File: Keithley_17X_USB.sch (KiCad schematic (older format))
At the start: 37 parts, among them J1 USB_B, J2 SIGNAL INPUT, J3 PROG, U1 TLP281-4, U2 TLP281-4, U3 MIC5504-3.3YM5, U4 MSP430FR2110, U5 FT230XS

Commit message: add more footprints and 3d models
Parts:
- D1: footprint (none) -> TI_TVSDiode:TI_PX1SON_DPY
- D3: value D_Schottky -> DSS16UTR; footprint (none) -> SMC_Diodes:D_SOD-123FL
- H1, H2, H3, H4: value CaseMnt -> M3
- J2: footprint (none) -> Connector_PinHeader_2.54mm:PinHeader_2x07_P2.54mm_Horizontal
- J3: footprint (none) -> Connector_PinHeader_2.54mm:PinHeader_1x04_P2.54mm_Vertical
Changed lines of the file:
@@
 P 2350 1000
 F 0 "D3" H 2350 1100 50  0000 C CNN
-F 1 "D_Schottky" H 2350 900 50  0000 C CNN
-F 2 "" H 2350 1000 50  0001 C CNN
+F 1 "DSS16UTR" H 2350 900 50  0000 C CNN
+F 2 "SMC_Diodes:D_SOD-123FL" H 2350 1000 50  0001 C CNN
 F 3 "http://www.smc-diodes.com/propdf/DSS12U%20THRU%20DSS125U%20N1873%20REV.A.pdf" H 2350 1000 50  0001 C CNN
 F 4 "SCHOTTKY 60V SOD-123FL" H 2350 1000 50  0001 C CNN "Description"
@@
 F 0 "D1" V 1250 1950 50  0000 C CNN
 F 1 "TPD1E10B06" H 1250 1750 50  0000 C CNN
-F 2 "" H 1250 1850 50  0001 C CNN
+F 2 "TI_TVSDiode:TI_PX1SON_DPY" H 1250 1850 50  0001 C CNN
 F 3 "http://www.ti.com/lit/ds/symlink/tpd1e10b06-q1.pdf" H 1250 1850 50  0001 C CNN
 F 4 "TVS DIODE 5.5V 14V 2X1SON" H 1250 1850 50  0001 C CNN "Description"
@@
 F 0 "J2" H 1600 5500 50  0000 C CNN
 F 1 "SIGNAL INPUT" H 1600 4700 50  0000 C CNN
-F 2 "" H 1550 5100 50  0001 C CNN
+F 2 "Connector_PinHeader_2.54mm:PinHeader_2x07_P2.54mm_Horizontal" H 1550 5100 50  0001 C CNN
 F 3 "http://www.on-shore.com/wp-content/uploads/2015/09/302-rxxx.pdf" H 1550 5100 50  0001 C CNN
 F 4 "CONN HEADER R/A 14POS 2.54MM" H 1550 5100 50  0001 C CNN "Description"
@@
 F 0 "J3" H 4950 3850 50  0000 C CNN
 F 1 "PROG" H 4950 3350 50  0000 C CNN
-F 2 "" H 4950 3650 50  0001 C CNN
+F 2 "Connector_PinHeader_2.54mm:PinHeader_1x04_P2.54mm_Vertical" H 4950 3650 50  0001 C CNN
 F 3 "~" H 4950 3650 50  0001 C CNN
 	1    4950 3650
@@
 P 5300 5950
 F 0 "H1" H 5300 6200 50  0000 C CNN
-F 1 "CaseMnt" H 5300 6125 50  0000 C CNN
+F 1 "M3" H 5300 6125 50  0000 C CNN
 F 2 "" H 5300 5950 50  0001 C CNN
 F 3 "~" H 5300 5950 50  0001 C CNN
@@
 P 5700 5950
 F 0 "H2" H 5700 6200 50  0000 C CNN
-F 1 "CaseMnt" H 5700 6125 50  0000 C CNN
+F 1 "M3" H 5700 6125 50  0000 C CNN
 F 2 "" H 5700 5950 50  0001 C CNN
 F 3 "~" H 5700 5950 50  0001 C CNN
@@
 P 6100 5950
 F 0 "H3" H 6100 6200 50  0000 C CNN
-F 1 "CaseMnt" H 6100 6125 50  0000 C CNN
+F 1 "M3" H 6100 6125 50  0000 C CNN
 F 2 "" H 6100 5950 50  0001 C CNN
 F 3 "~" H 6100 5950 50  0001 C CNN
@@
 P 6500 5950
 F 0 "H4" H 6500 6200 50  0000 C CNN
-F 1 "CaseMnt" H 6500 6125 50  0000 C CNN
+F 1 "M3" H 6500 6125 50  0000 C CNN
 F 2 "" H 6500 5950 50  0001 C CNN
 F 3 "~" H 6500 5950 50  0001 C CNN

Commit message: add r_array footprint and 3d model
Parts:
- H1, H2, H3, H4: footprint (none) -> MountingHole:MountingHole_3.2mm_M3_DIN965_Pad
- RN1, RN2: footprint (none) -> R_Array_Convex:YC324-JK-0710KL
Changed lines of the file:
@@
 F 0 "RN1" V 2250 4650 50  0000 C CNN
 F 1 "10k" V 2750 4650 50  0000 C CNN
-F 2 "" V 2825 4650 50  0001 C CNN
+F 2 "R_Array_Convex:YC324-JK-0710KL" V 2825 4650 50  0001 C CNN
 F 3 "https://media.digikey.com/pdf/Data%20Sheets/Yageo%20PDFs/YC102-358,TC122-164_Series_DS.pdf" H 2550 4650 50  0001 C CNN
 F 4 "RES ARRAY 4 RES 10K OHM 2012" H 2550 4650 50  0001 C CNN "Description"
@@
 F 0 "RN2" V 2250 7450 50  0000 C CNN
 F 1 "10k" V 2750 7450 50  0000 C CNN
-F 2 "" V 2825 7450 50  0001 C CNN
+F 2 "R_Array_Convex:YC324-JK-0710KL" V 2825 7450 50  0001 C CNN
 F 3 "https://media.digikey.com/pdf/Data%20Sheets/Yageo%20PDFs/YC102-358,TC122-164_Series_DS.pdf" H 2550 7450 50  0001 C CNN
 F 4 "RES ARRAY 4 RES 10K OHM 2012" H 2550 7450 50  0001 C CNN "Description"
@@
 F 0 "H1" H 5300 6200 50  0000 C CNN
 F 1 "M3" H 5300 6125 50  0000 C CNN
-F 2 "" H 5300 5950 50  0001 C CNN
+F 2 "MountingHole:MountingHole_3.2mm_M3_DIN965_Pad" H 5300 5950 50  0001 C CNN
 F 3 "~" H 5300 5950 50  0001 C CNN
 	1    5300 5950
@@
 F 0 "H2" H 5700 6200 50  0000 C CNN
 F 1 "M3" H 5700 6125 50  0000 C CNN
-F 2 "" H 5700 5950 50  0001 C CNN
+F 2 "MountingHole:MountingHole_3.2mm_M3_DIN965_Pad" H 5700 5950 50  0001 C CNN
 F 3 "~" H 5700 5950 50  0001 C CNN
 	1    5700 5950
@@
 F 0 "H3" H 6100 6200 50  0000 C CNN
 F 1 "M3" H 6100 6125 50  0000 C CNN
-F 2 "" H 6100 5950 50  0001 C CNN
+F 2 "MountingHole:MountingHole_3.2mm_M3_DIN965_Pad" H 6100 5950 50  0001 C CNN
 F 3 "~" H 6100 5950 50  0001 C CNN
 	1    6100 5950
@@
 F 0 "H4" H 6500 6200 50  0000 C CNN
 F 1 "M3" H 6500 6125 50  0000 C CNN
-F 2 "" H 6500 5950 50  0001 C CNN
+F 2 "MountingHole:MountingHole_3.2mm_M3_DIN965_Pad" H 6500 5950 50  0001 C CNN
 F 3 "~" H 6500 5950 50  0001 C CNN
 	1    6500 5950

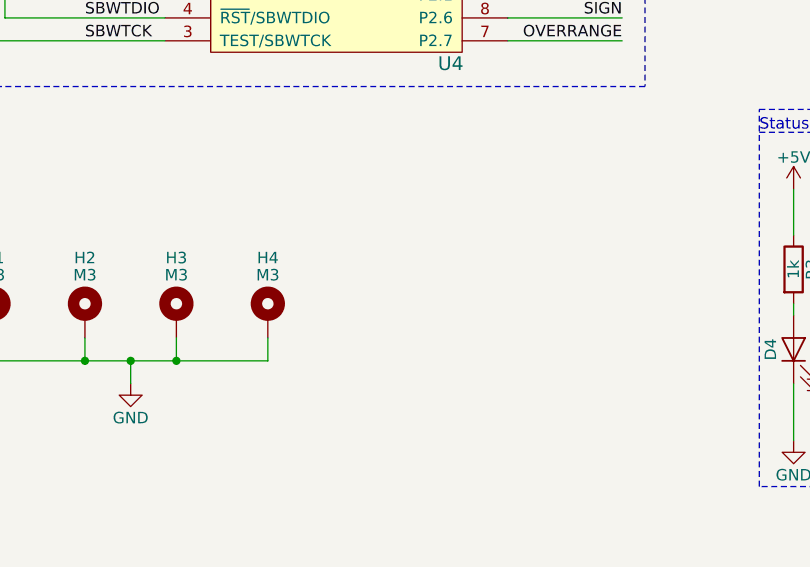
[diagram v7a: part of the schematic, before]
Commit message: add right angle mounting holes
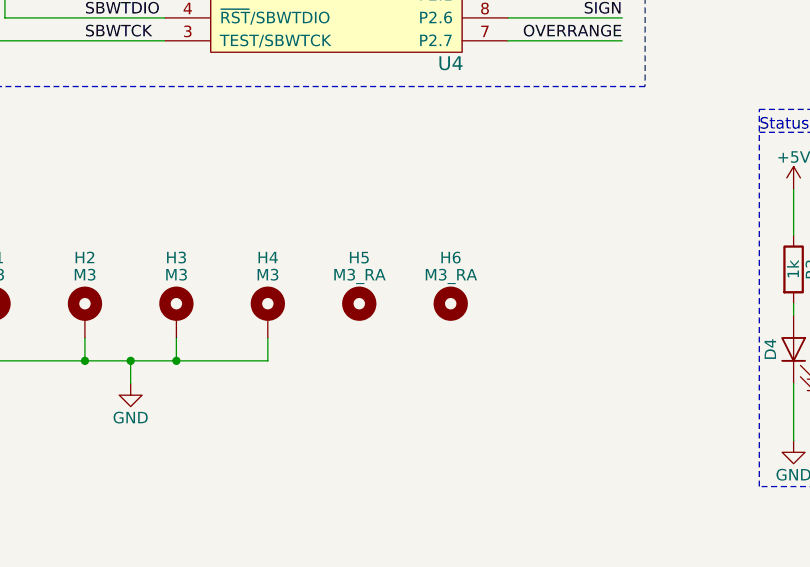
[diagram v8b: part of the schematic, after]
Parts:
- added H5, H6: M3_RA, symbol Mechanical:MountingHole
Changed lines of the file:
@@
 Wire Wire Line
 	5500 7450 5500 7500
+$Comp
+L Mechanical:MountingHole H5
+U 1 1 5C6C1140
+P 6900 5900
+F 0 "H5" H 6900 6100 50  0000 C CNN
+F 1 "M3_RA" H 6900 6025 50  0000 C CNN
+F 2 "" H 6900 5900 50  0001 C CNN
+F 3 "~" H 6900 5900 50  0001 C CNN
+	1    6900 5900
+	1    0    0    -1
+$EndComp
+$Comp
+L Mechanical:MountingHole H6
+U 1 1 5C6C11B3
+P 7300 5900
+F 0 "H6" H 7300 6100 50  0000 C CNN
+F 1 "M3_RA" H 7300 6025 50  0000 C CNN
+F 2 "" H 7300 5900 50  0001 C CNN
+F 3 "~" H 7300 5900 50  0001 C CNN
+	1    7300 5900
+	1    0    0    -1
+$EndComp
 $EndSCHEMATC
